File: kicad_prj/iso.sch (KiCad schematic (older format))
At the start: 15 parts

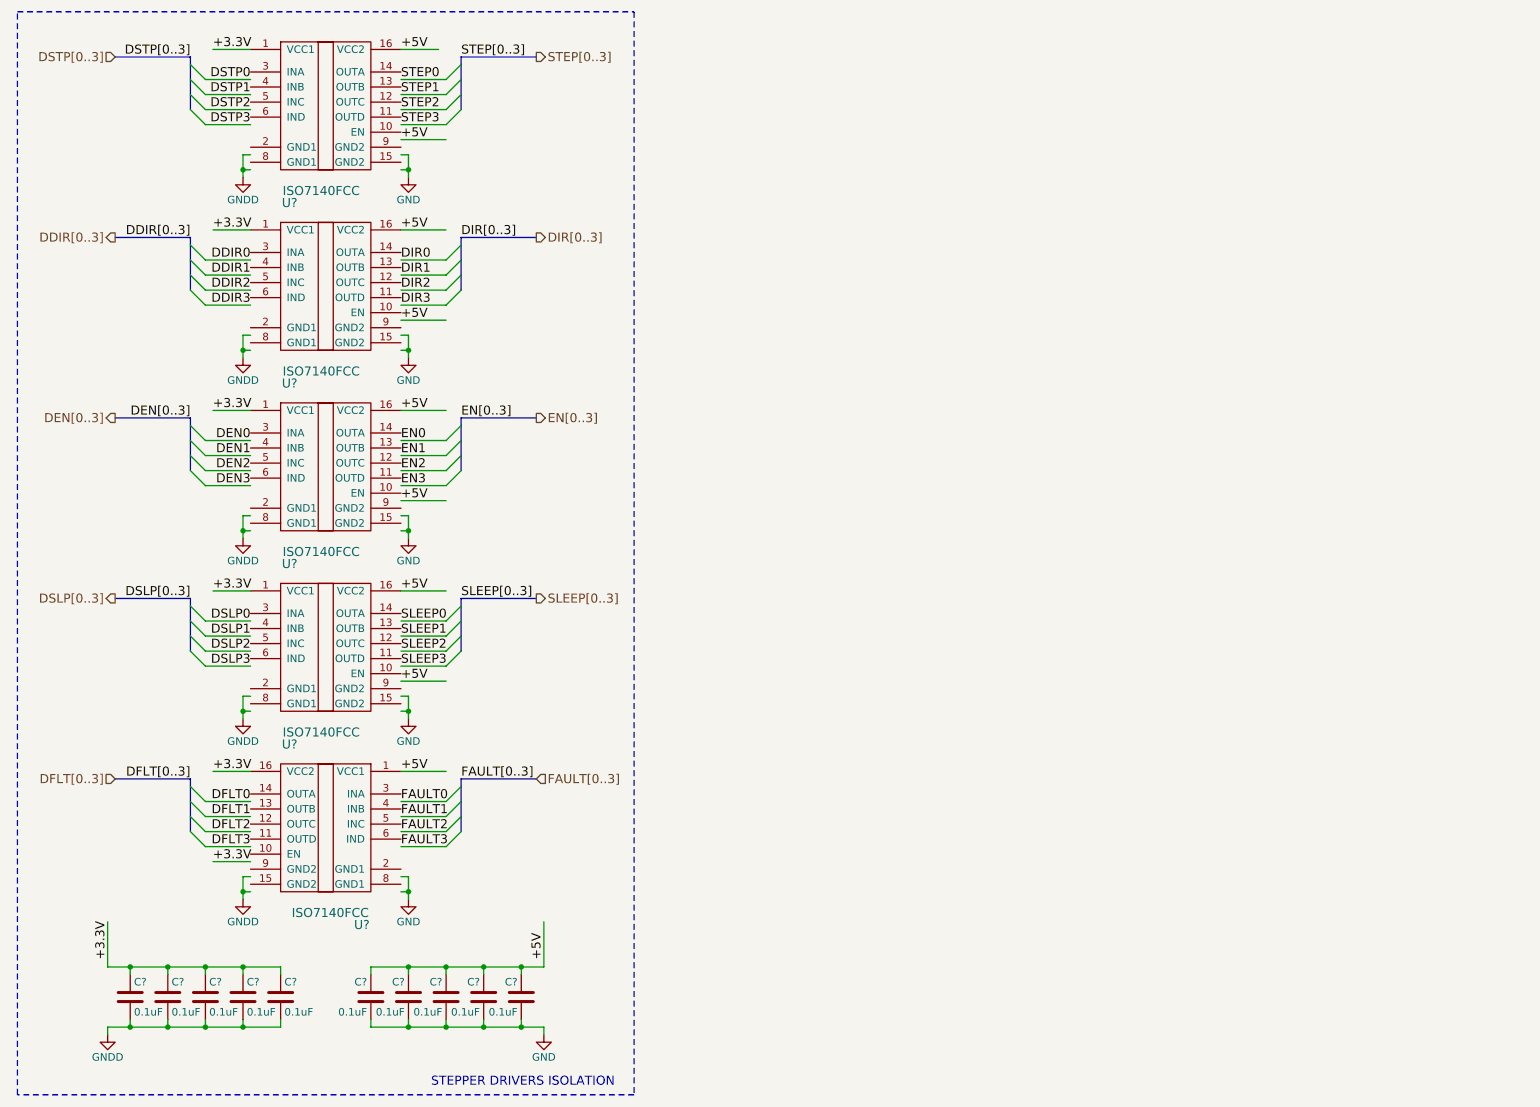
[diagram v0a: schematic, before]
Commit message: Schematics 6
Added isolation.
Misc. i2c, I/Os, spi. Need to finish iso2 sheet.
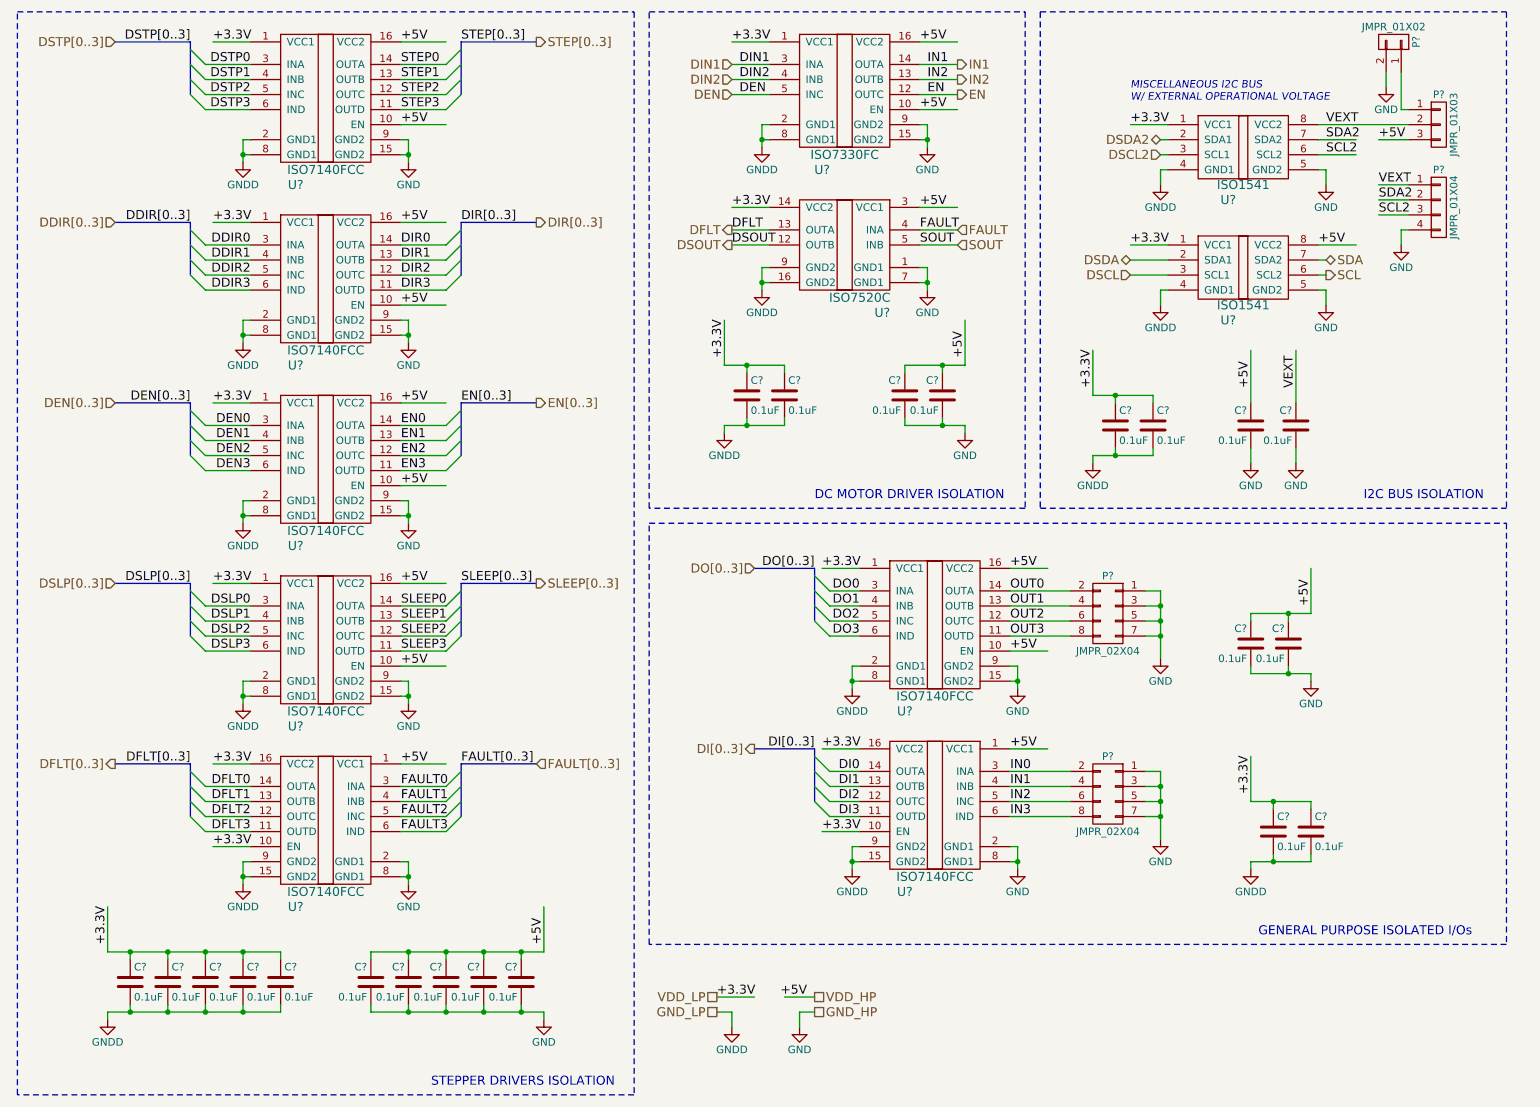
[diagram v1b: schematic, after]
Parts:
- added C? (x12): 0.1uF, symbol C
- added P?: JMPR_01X04, symbol JMPR_01X04
- added P? (x2): JMPR_02X04, symbol JMPR_02X04
- added P?: JMPR_01X03, symbol JMPR_01X03
- added P?: JMPR_01X02, symbol JMPR_01X02
- added U? (x2): ISO7140FCC, symbol ISO7140FCC
- added U?: ISO7330FC, symbol ISO7330FC
- added U?: ISO7520C, symbol ISO7520C
- added U? (x2): ISO1541, symbol ISO1541
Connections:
- net labels added: DEN, DFLT, DI0, DI1, DI2, DI3, DIN1, DIN2, DI[0..3], DO0, DO1, DO2, DO3, DO[0..3], DSCL, DSCL2, DSDA, DSDA2, DSOUT, EN, FAULT, GND_HP, GND_LP, IN0, IN1, IN2, IN3, OUT0, OUT1, OUT2, OUT3, SCL, SCL2, SDA, SDA2, SOUT, VDD_HP, VDD_LP, VEXT
- wire segments 113 -> 263
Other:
- note added: "DC MOTOR DRIVER ISOLATION"
- note added: "GENERAL PURPOSE ISOLATED I/Os"
- note added: "I2C BUS ISOLATION"
- note added: "MISCELLANEOUS I2C BUS\nW/ EXTERNAL OPERATIONAL VOLTAGE"
- moved on the sheet: C?, U?

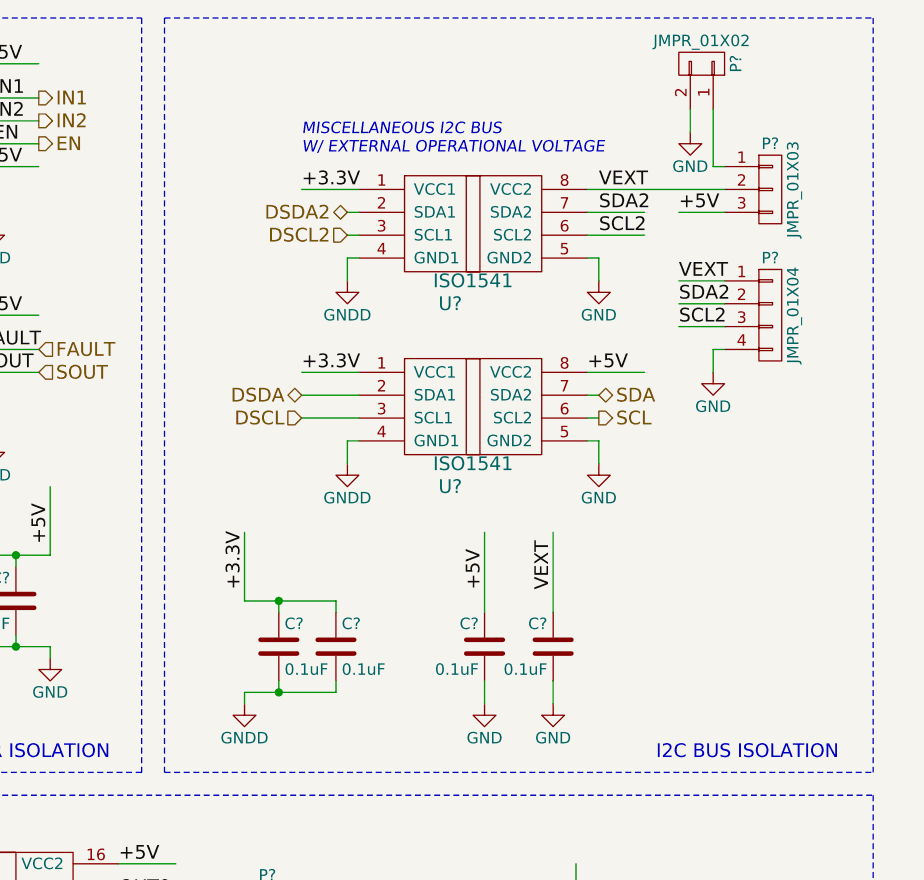
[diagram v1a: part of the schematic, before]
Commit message: Schematics 7
Started power schematics.
Need to:
- correct symbol for sw vreg
- add regulator for 3.3V digital side
- indicate which voltages go to which circuit
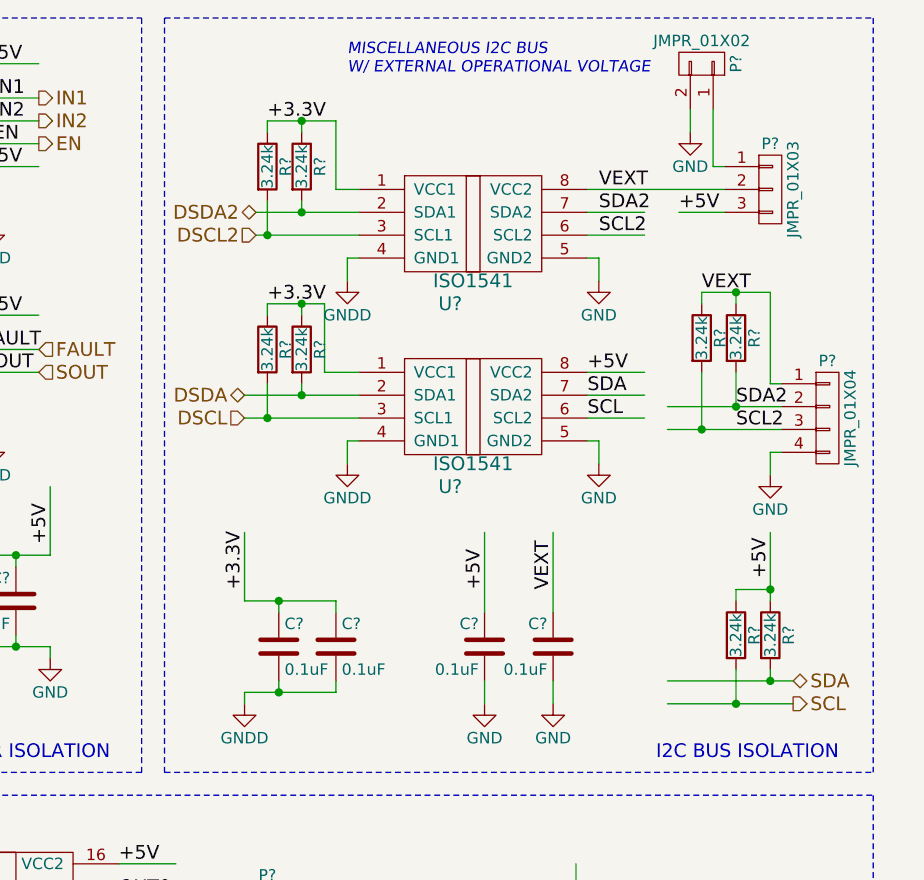
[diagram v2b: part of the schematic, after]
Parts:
- added R? (x8): 3.24k, symbol R
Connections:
- wire segments 263 -> 288
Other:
- moved on the sheet: P?
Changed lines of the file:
@@
 $Descr A 11000 8500
 encoding utf-8
-Sheet 9 10
+Sheet 9 11
 Title ""
 Date ""
@@
 	1    0    0    -1
 $EndComp
-Text Label 7900 1250 0    60   ~ 0
+Text Label 7750 950  0    60   ~ 0
 +3.3V
-Text Label 7900 2050 0    60   ~ 0
+Text Label 7750 1750 0    60   ~ 0
 +3.3V
 Text Label 9550 1350 0    60   ~ 0
@@
 Text Label 9200 1250 0    60   ~ 0
 VEXT
-Text HLabel 9200 2150 2    60   BiDi ~ 0
+Text HLabel 10050 3400 2    60   BiDi ~ 0
 SDA
-Text HLabel 9200 2250 2    60   Output ~ 0
+Text HLabel 10050 3500 2    60   Output ~ 0
 SCL
-Text HLabel 7900 2150 0    60   BiDi ~ 0
+Text HLabel 7650 2150 0    60   BiDi ~ 0
 DSDA
-Text HLabel 7900 2250 0    60   Input ~ 0
+Text HLabel 7650 2250 0    60   Input ~ 0
 DSCL
-Text HLabel 8100 1450 0    60   Input ~ 0
+Text HLabel 7700 1450 0    60   Input ~ 0
 DSCL2
-Text HLabel 8100 1350 0    60   BiDi ~ 0
+Text HLabel 7700 1350 0    60   BiDi ~ 0
 DSDA2
 Text Label 9200 1350 0    60   ~ 0
@@
 Text Label 9200 1450 0    60   ~ 0
 SCL2
-Text Notes 7900 1100 0    50   Italic 0
+Text Notes 8100 750  0    50   Italic 0
 MISCELLANEOUS I2C BUS\nW/ EXTERNAL OPERATIONAL VOLTAGE
 Text Notes 9450 3750 0    60   ~ 0
@@
 L JMPR_01X04 P?
 U 1 1 565A7C03
-P 9950 1800
-F 0 "P?" H 9950 2050 50  0000 C CNN
-F 1 "JMPR_01X04" V 10050 1800 50  0000 C CNN
-F 2 "" H 9950 1800 60  0000 C CNN
-F 3 "" H 9950 1800 60  0000 C CNN
-	1    9950 1800
+P 10200 2250
+F 0 "P?" H 10200 2500 50  0000 C CNN
+F 1 "JMPR_01X04" V 10300 2250 50  0000 C CNN
+F 2 "" H 10200 2250 60  0000 C CNN
+F 3 "" H 10200 2250 60  0000 C CNN
+	1    10200 2250
 	1    0    0    -1
 $EndComp
@@
 L GND #PWR?
 U 1 1 565A8333
-P 9700 2050
-F 0 "#PWR?" H 9700 1800 50  0001 C CNN
-F 1 "GND" H 9700 1900 50  0000 C CNN
-F 2 "" H 9700 2050 60  0000 C CNN
-F 3 "" H 9700 2050 60  0000 C CNN
-	1    9700 2050
-	1    0    0    -1
-$EndComp
-Text Label 9550 1650 0    60   ~ 0
+P 9950 2500
+F 0 "#PWR?" H 9950 2250 50  0001 C CNN
+F 1 "GND" H 9950 2350 50  0000 C CNN
+F 2 "" H 9950 2500 60  0000 C CNN
+F 3 "" H 9950 2500 60  0000 C CNN
+	1    9950 2500
+	1    0    0    -1
+$EndComp
+Text Label 9650 1700 0    60   ~ 0
 VEXT
-Text Label 9550 1750 0    60   ~ 0
+Text Label 9800 2200 0    60   ~ 0
 SDA2
-Text Label 9550 1850 0    60   ~ 0
+Text Label 9800 2300 0    60   ~ 0
 SCL2
 $Comp
@@
 	8100 2350 8100 2450
 Wire Wire Line
-	7900 1250 8150 1250
-Wire Wire Line
-	7900 2050 8150 2050
-Wire Wire Line
 	9550 1350 9750 1350
 Wire Wire Line
 	9150 2050 9400 2050
 Wire Wire Line
-	9150 2150 9200 2150
-Wire Wire Line
-	9150 2250 9200 2250
-Wire Wire Line
-	8150 2150 7900 2150
-Wire Wire Line
-	8150 2250 7900 2250
+	9150 2150 9400 2150
+Wire Wire Line
+	9150 2250 9400 2250
+Wire Wire Line
+	8150 2150 7650 2150
+Wire Wire Line
+	8150 2250 7650 2250
 Wire Wire Line
 	9150 1350 9400 1350
@@
 	9150 1450 9400 1450
 Wire Wire Line
-	8150 1350 8100 1350
-Wire Wire Line
-	8150 1450 8100 1450
+	8150 1350 7700 1350
+Wire Wire Line
+	8150 1450 7700 1450
 Wire Wire Line
 	8700 3100 8700 2750
@@
 	7300 3800 10400 3800
 Wire Notes Line
-	9900 3100 9900 3100
+	9850 3450 9850 3450
 Wire Wire Line
 	9000 3100 9000 2750
@@
 	9150 1250 9750 1250
 Wire Wire Line
-	9750 1650 9550 1650
-Wire Wire Line
-	9750 1750 9550 1750
-Wire Wire Line
-	9750 1850 9550 1850
-Wire Wire Line
-	9750 1950 9700 1950
-Wire Wire Line
-	9700 1950 9700 2050
+	9500 2200 10000 2200
+Wire Wire Line
+	9500 2300 10000 2300
+Wire Wire Line
+	10000 2400 9950 2400
+Wire Wire Line
+	9950 2400 9950 2500
 Wire Wire Line
 	7100 4350 7500 4350
@@
 Text Label 5150 7050 0    60   ~ 0
 +3.3V
+$Comp
+L R R?
+U 1 1 565F488C
+P 9950 3200
+F 0 "R?" V 10030 3200 50  0000 C CNN
+F 1 "3.24k" V 9950 3200 50  0000 C CNN
+F 2 "" V 9880 3200 30  0000 C CNN
+F 3 "" H 9950 3200 30  0000 C CNN
+	1    9950 3200
+	1    0    0    -1
+$EndComp
+$Comp
+L R R?
+U 1 1 565F607D
+P 9650 1900
+F 0 "R?" V 9730 1900 50  0000 C CNN
+F 1 "3.24k" V 9650 1900 50  0000 C CNN
+F 2 "" V 9580 1900 30  0000 C CNN
+F 3 "" H 9650 1900 30  0000 C CNN
+	1    9650 1900
+	1    0    0    -1
+$EndComp
+$Comp
+L R R?
+U 1 1 565F6109
+P 9800 1900
+F 0 "R?" V 9880 1900 50  0000 C CNN
+F 1 "3.24k" V 9800 1900 50  0000 C CNN
+F 2 "" V 9730 1900 30  0000 C CNN
+F 3 "" H 9800 1900 30  0000 C CNN
+	1    9800 1900
+	1    0    0    -1
+$EndComp
+$Comp
+L R R?
+U 1 1 565F61A0
+P 9800 3200
+F 0 "R?" V 9880 3200 50  0000 C CNN
+F 1 "3.24k" V 9800 3200 50  0000 C CNN
+F 2 "" V 9730 3200 30  0000 C CNN
+F 3 "" H 9800 3200 30  0000 C CNN
+	1    9800 3200
+	1    0    0    -1
+$EndComp
+Wire Wire Line
+	9500 3400 10050 3400
+Wire Wire Line
+	9500 3500 10050 3500
+Wire Wire Line
+	9800 3350 9800 3500
+Connection ~ 9800 3500
+Wire Wire Line
+	9950 3350 9950 3400
+Connection ~ 9950 3400
+Text Label 9150 2150 0    60   ~ 0
+SDA
+Text Label 9150 2250 0    60   ~ 0
+SCL
+Wire Wire Line
+	9950 2750 9950 3050
+Wire Wire Line
+	9800 3050 9800 3000
+Wire Wire Line
+	9800 3000 9950 3000
+Connection ~ 9950 3000
+Text Label 9950 2950 1    60   ~ 0
++5V
+Wire Wire Line
+	9800 2050 9800 2200
+Connection ~ 9800 2200
+Wire Wire Line
+	9650 2050 9650 2300
+Connection ~ 9650 2300
+Wire Wire Line
+	9650 1750 9650 1700
+Wire Wire Line
+	9650 1700 9950 1700
+Wire Wire Line
+	9950 1700 9950 2100
+Wire Wire Line
+	9950 2100 10000 2100
+Wire Wire Line
+	9800 1750 9800 1700
+Connection ~ 9800 1700
+$Comp
+L R R?
+U 1 1 56604E68
+P 7750 1950
+F 0 "R?" V 7830 1950 50  0000 C CNN
+F 1 "3.24k" V 7750 1950 50  0000 C CNN
+F 2 "" V 7680 1950 30  0000 C CNN
+F 3 "" H 7750 1950 30  0000 C CNN
+	1    7750 1950
+	1    0    0    -1
+$EndComp
+$Comp
+L R R?
+U 1 1 56604E6E
+P 7900 1950
+F 0 "R?" V 7980 1950 50  0000 C CNN
+F 1 "3.24k" V 7900 1950 50  0000 C CNN
+F 2 "" V 7830 1950 30  0000 C CNN
+F 3 "" H 7900 1950 30  0000 C CNN
+	1    7900 1950
+	1    0    0    -1
+$EndComp
+$Comp
+L R R?
+U 1 1 56604F48
+P 7750 1150
+F 0 "R?" V 7830 1150 50  0000 C CNN
+F 1 "3.24k" V 7750 1150 50  0000 C CNN
+F 2 "" V 7680 1150 30  0000 C CNN
+F 3 "" H 7750 1150 30  0000 C CNN
+	1    7750 1150
+	1    0    0    -1
+$EndComp
+$Comp
+L R R?
+U 1 1 56604F4E
+P 7900 1150
+F 0 "R?" V 7980 1150 50  0000 C CNN
+F 1 "3.24k" V 7900 1150 50  0000 C CNN
+F 2 "" V 7830 1150 30  0000 C CNN
+F 3 "" H 7900 1150 30  0000 C CNN
+	1    7900 1150
+	1    0    0    -1
+$EndComp
+Wire Wire Line
+	7750 2100 7750 2250
+Connection ~ 7750 2250
+Wire Wire Line
+	7900 2100 7900 2150
+Connection ~ 7900 2150
+Wire Wire Line
+	7750 1300 7750 1450
+Connection ~ 7750 1450
+Wire Wire Line
+	7900 1300 7900 1350
+Connection ~ 7900 1350
+Wire Wire Line
+	7750 1000 7750 950
+Wire Wire Line
+	7750 950  8050 950
+Wire Wire Line
+	8050 950  8050 1250
+Wire Wire Line
+	8050 1250 8150 1250
+Wire Wire Line
+	7900 1000 7900 950
+Connection ~ 7900 950
+Wire Wire Line
+	7750 1800 7750 1750
+Wire Wire Line
+	7750 1750 8000 1750
+Wire Wire Line
+	8000 1750 8000 2050
+Wire Wire Line
+	8000 2050 8150 2050
+Wire Wire Line
+	7900 1800 7900 1750
+Connection ~ 7900 1750
 $EndSCHEMATC
